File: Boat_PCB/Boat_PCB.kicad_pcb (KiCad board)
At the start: 2 copper layers, 140 x 98 mm, 45 parts, among them J1 Conn_02x06_Odd_Even, J11 Temp + Humidity Sensor Extern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, J12 led GPIO 12, J13 Temp + Humidity Sensor Intern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, J14 Conn_01x20_Socket, J15 Hull Leak Right GPIO 20, J16 Hull Leak Left GPIO 19, J17 Conn_01x20_Socket, J18 Stepper Motor, J2 Conn_01x03_Socket, J3 Raspberry Pi 5 connector, J4 12s Tap, J5 IMU 14,15 I2C 17,18 RST and I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, J6 4s output, J7 GPS + Compass GPIO 8,9 +15,14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, J8 Winch ESC GPIO 21, J9 Winch ESC RC, U1 MCP2515-I_P, U2 TJA1051T-3, Y1 Crystal

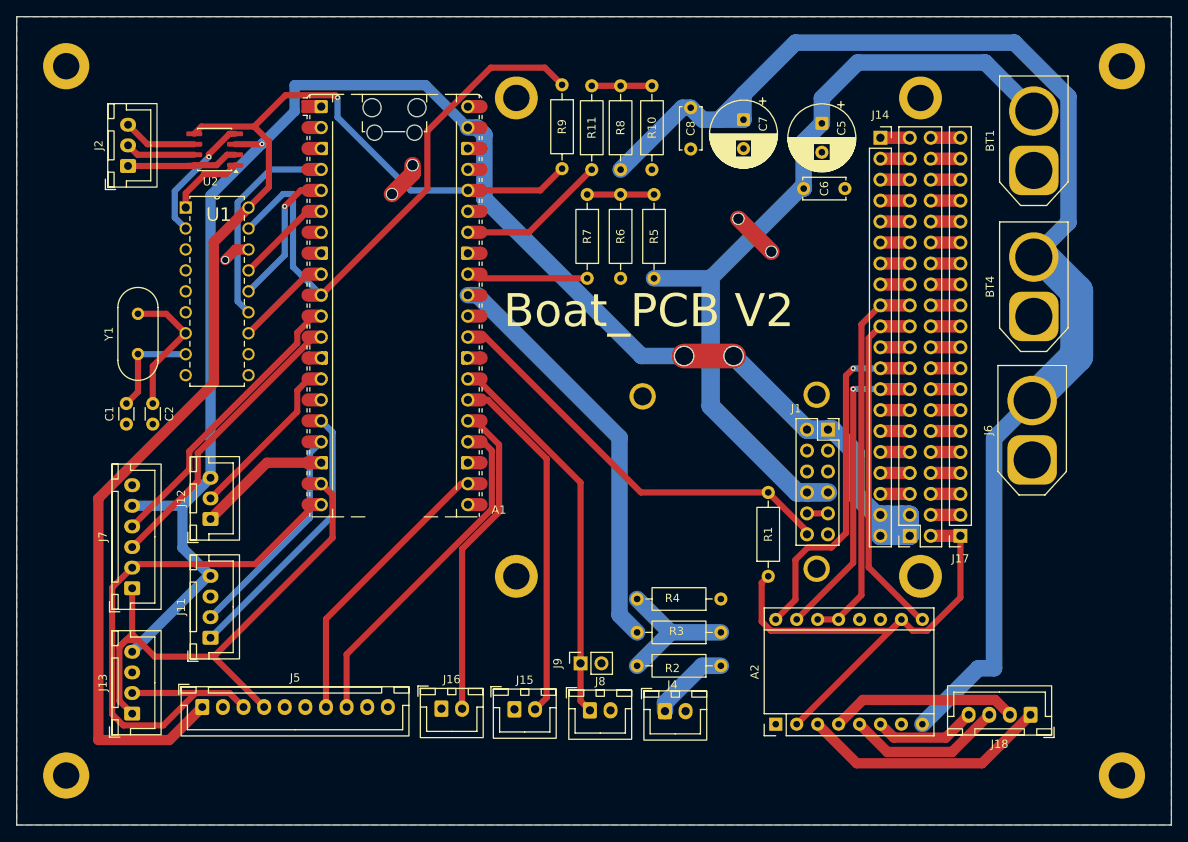
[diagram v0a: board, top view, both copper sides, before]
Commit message: Add three-tier survey vision pipeline with threat tracking
Layers a cheap water-segmentation anomaly screen (Tier 1) in front of
the existing YOLO overlay (Tier 2, now gated on anomaly), plus a threat
assessor (Tier 3) that turns detections into distance/approach-vector
radar tracking and mission alerts. Adds config, tests, and updates the
command center UI and hardware runner to wire it in. Also captures the
KiCad schematic/PCB updates from the M18 battery migration and refreshes
the session journal.
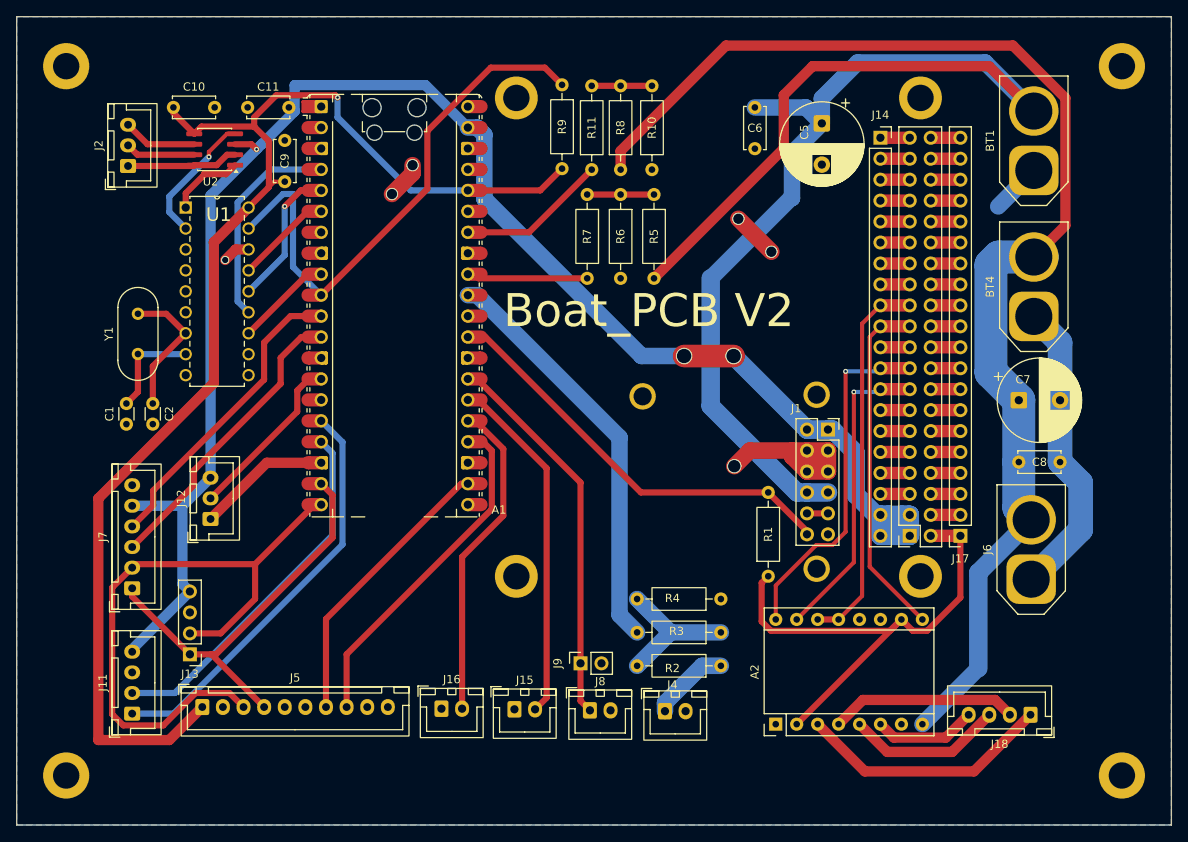
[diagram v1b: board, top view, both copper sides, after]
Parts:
- added C10: C, Capacitor_THT:C_Disc_D5.0mm_W2.5mm_P5.00mm, F.Cu at (65.0, 32.0)
- added C11: C, Capacitor_THT:C_Disc_D5.0mm_W2.5mm_P5.00mm, F.Cu at (74.0, 32.0)
- added C9: C, Capacitor_THT:C_Disc_D5.0mm_W2.5mm_P5.00mm, F.Cu at (78.5, 36.0)
- C5, C7: footprint Capacitor_THT:CP_Radial_D8.0mm_P3.50mm -> Capacitor_THT:CP_Radial_D10.0mm_P5.00mm
- J13: footprint Connector_JST:JST_XH_B4B-XH-A_1x04_P2.50mm_Vertical -> Connector_PinHeader_2.54mm:PinHeader_1x04_P2.54mm_Vertical
- moved C8 58.5 mm to (167.5, 75.0), turned to 0 degrees
- moved C7 47.7 mm to (167.5, 67.5), turned to 0 degrees
- moved J6 14.5 mm to (169.0, 89.2)
- moved J11 13.2 mm to (60.0, 105.5)
- moved C6 11.5 mm to (135.5, 32.0), turned to -90 degrees
- moved J13 10.0 mm to (67.0, 98.3), turned to 180 degrees
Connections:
- J14 pad 11: Net-(J14-Pin_11) -> GND
- J17 pad 5: Net-(J17-Pin_5) -> GND
- J3 pad 10: Net-(J17-Pin_5) -> GND
- J3 pad 19: Net-(J14-Pin_11) -> GND
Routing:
- net GND: track 50.5 -> 133.2 mm, vias 5 -> 6
- net Net-(BT1--): track 98.5 -> 163.2 mm
- net Net-(A1-GPIO13): track 26.8 -> 44.1 mm
- net Net-(A1-GPIO12): track 33.0 -> 50.1 mm
- net Net-(A1-GPIO14): track 66.3 -> 50.2 mm
- net Net-(A1-3V3): track 151.7 -> 158.8 mm
- net Net-(A1-GPIO15): track 70.6 -> 76.7 mm
- net Net-(A2-VMOT): track 160.1 -> 154.8 mm
- net Net-(J17-Pin_5): track 3.60 -> 0.00 mm
- net Net-(J14-Pin_11): track 3.56 -> 0.00 mm
- net Net-(A1-GPIO9): track 34.7 -> 36.5 mm
- net Net-(A1-VSYS): track 210.7 -> 209.0 mm
- net Net-(A1-GPIO8): track 35.5 -> 37.2 mm
- net Net-(A2-1B): track 30.2 -> 31.0 mm
- net Net-(U1-RXCAN): track 15.5 -> 16.2 mm
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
